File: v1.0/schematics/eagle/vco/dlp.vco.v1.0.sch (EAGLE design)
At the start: 101 parts, among them IC1 NTE912P, IC2 TL074P, IC3 4013N, IC4 TL074P, IC5 TL074P, IC7 TL074P, J1 PWM, J10 SW OUT, J2 LIN FM, J3 SQ OUT, J4 EXP FM, J5 PITCH, J6 SW OUT, J7 SUB OUT, J8 OSC1 OUT, J9 EXP FM, Q1 2N3417, Q2 2N3417, Q3 2N3906, Q4 2N3417, Q5 2N3417, Q6 2N3906

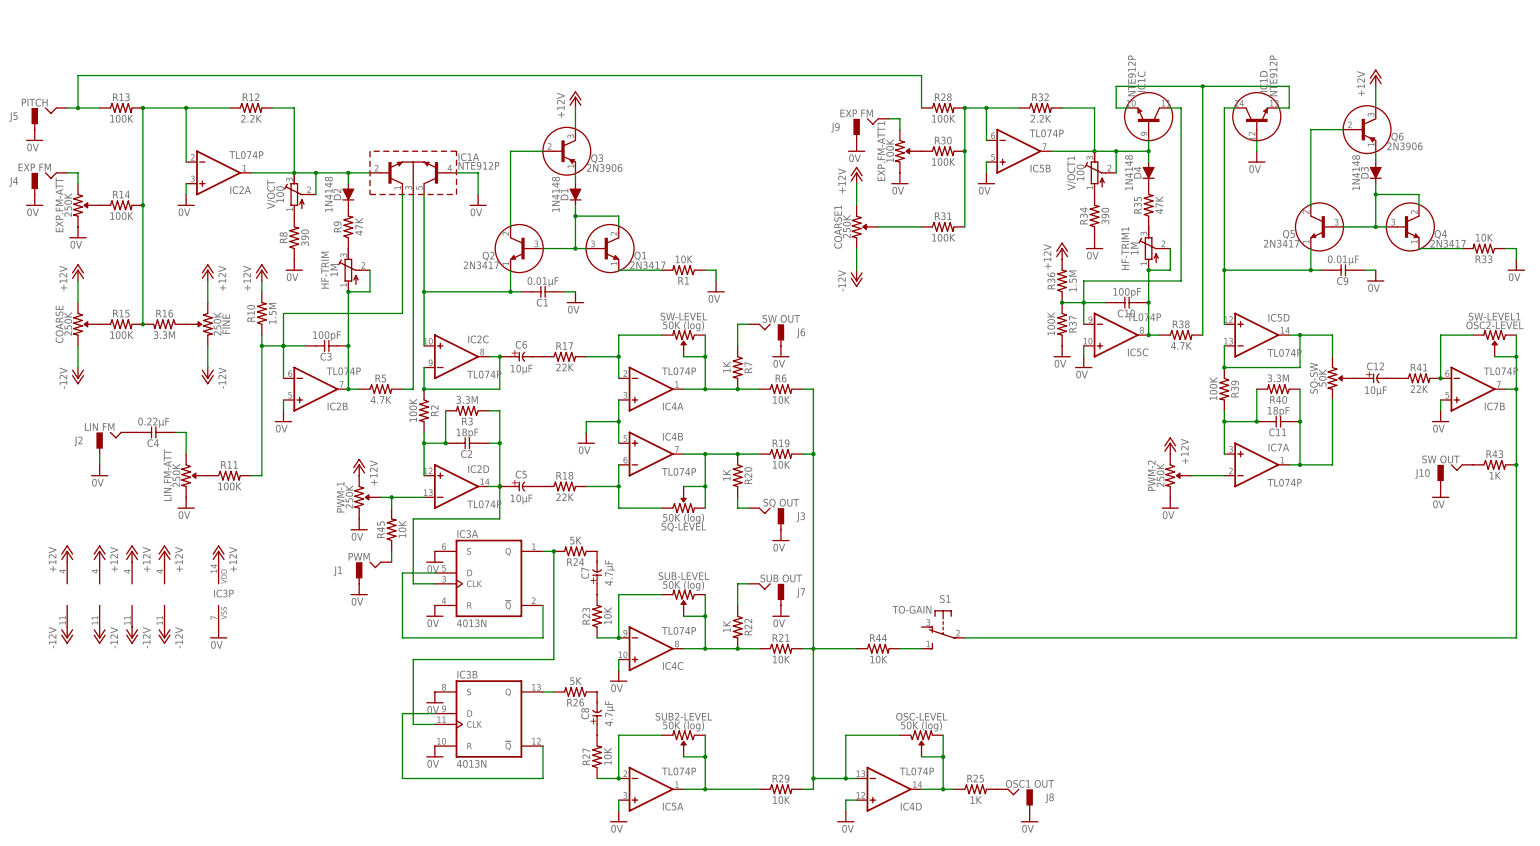
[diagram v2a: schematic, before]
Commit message: Refreshed ASDR pdf (removed png) Updated VCO values Added Pitch Link to VCO Replaced OSC2 LOG.FM with LIN.FM Updated PDF (removed png)
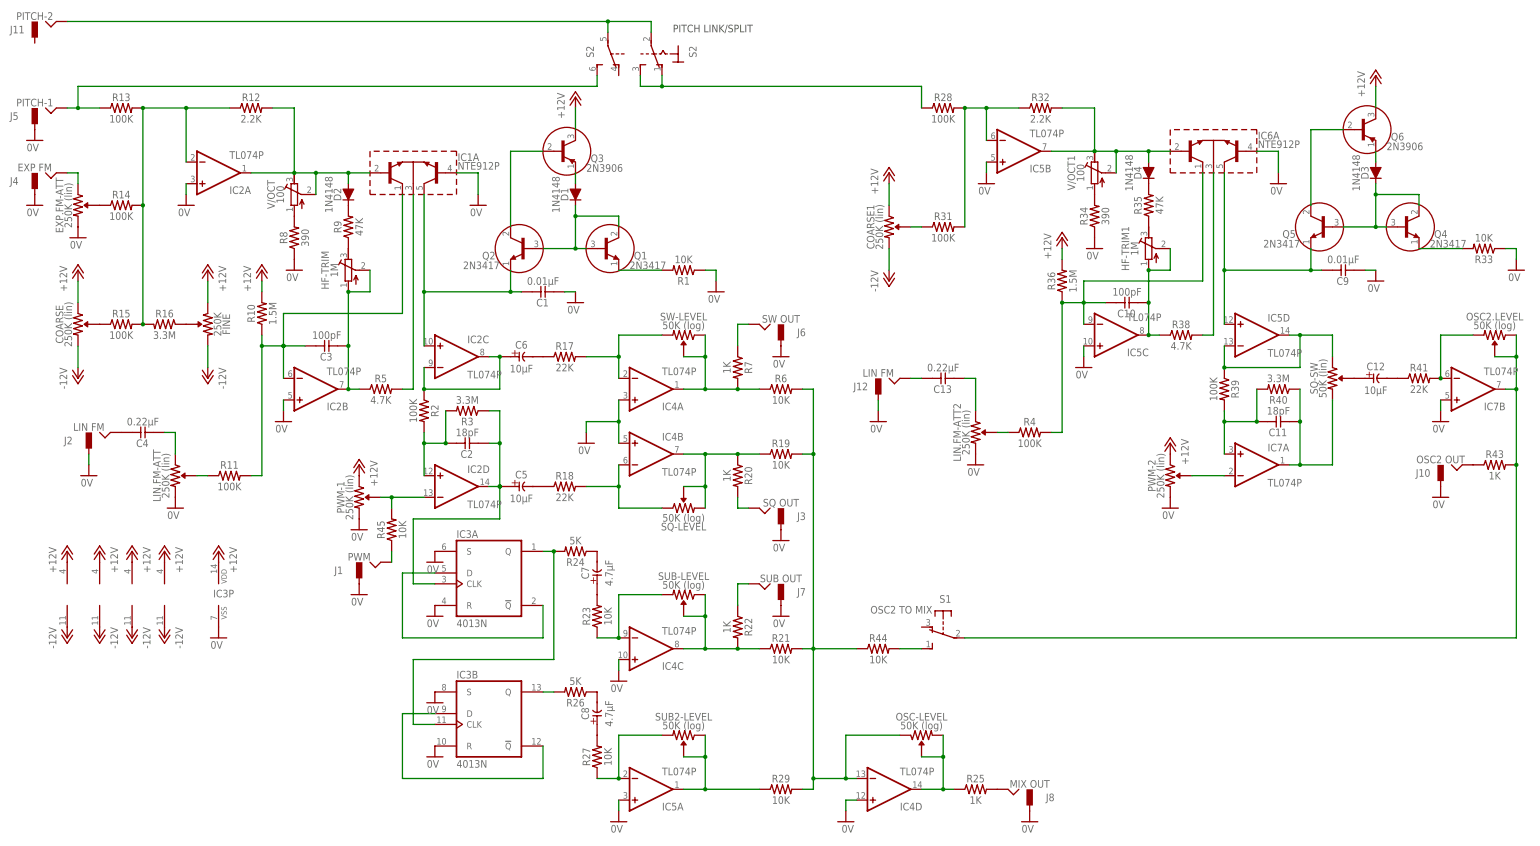
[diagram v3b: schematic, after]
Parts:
- removed EXP.FM-ATT1: 100K, _common:R-VAR
- removed J9: EXP FM, _common:JACK-M
- removed R30, R37: 100K, _common:R0309/10
- added C13: 0.22μF, _common:CC-US025-024X044
- added IC6: NTE912P, _common:NTE912P
- added J11: PITCH-2, _common:JACK-M
- added J12: LIN FM, _common:JACK-M
- added LIN.FM-ATT2: 250K (lin), _common:R-VAR
- added R4: 100K, _common:R0309/10
- added S2: (no value), switch:320-938
- COARSE, COARSE1, EXP.FM-ATT, LIN.FM-ATT, PWM-1, PWM-2: value 250K -> 250K (lin)
- J10: value SW OUT -> OSC2 OUT
- J5: value PITCH -> PITCH-1
- J8: value OSC1 OUT -> MIX OUT
- OSC2.LEVEL: value OSC2-LEVEL -> 50K (log)
- S1: value TO-GAIN -> OSC2 TO MIX
- SQ-SW: value 50K -> 50K (lin)
- renumbered SW-LEVEL1 to OSC2.LEVEL
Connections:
- removed net N$53: EXP.FM-ATT1.1, J9.HOT
- new net N$78: J5.HOT, R13.1, S2B.S
- new net N$79: R28.1, S21.O, S21.S
- new net N$80: LIN.FM-ATT2.P$1, R4.1
- new net N$81: C13.2, LIN.FM-ATT2.1
- net 0V: now also IC6A.B3, J12.GND, LIN.FM-ATT2.2; no longer EXP.FM-ATT1.2, IC1D.B, J9.GND, R37.2
- net N$27: now also J11.HOT, S21.P, S2B.P; no longer J5.HOT, R13.1, R28.1
- net N$51: now also C13.1, J12.HOT; no longer EXP.FM-ATT1.P$1, R30.1
- net N$54: no longer R30.2
- net N$56: no longer IC1D.C
- net N$62: now also IC6A.E; no longer IC1C.E, IC1D.E
- net N$64: now also R4.2; no longer IC1C.C, R37.1
- net N$65: now also IC6A.B1; no longer IC1C.B
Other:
- note added: "PITCH LINK/SPLIT"
- moved on the sheet: C4, COARSE1, J2, LIN.FM-ATT

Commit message: Updated VCO with revised values and added bypass capacitors
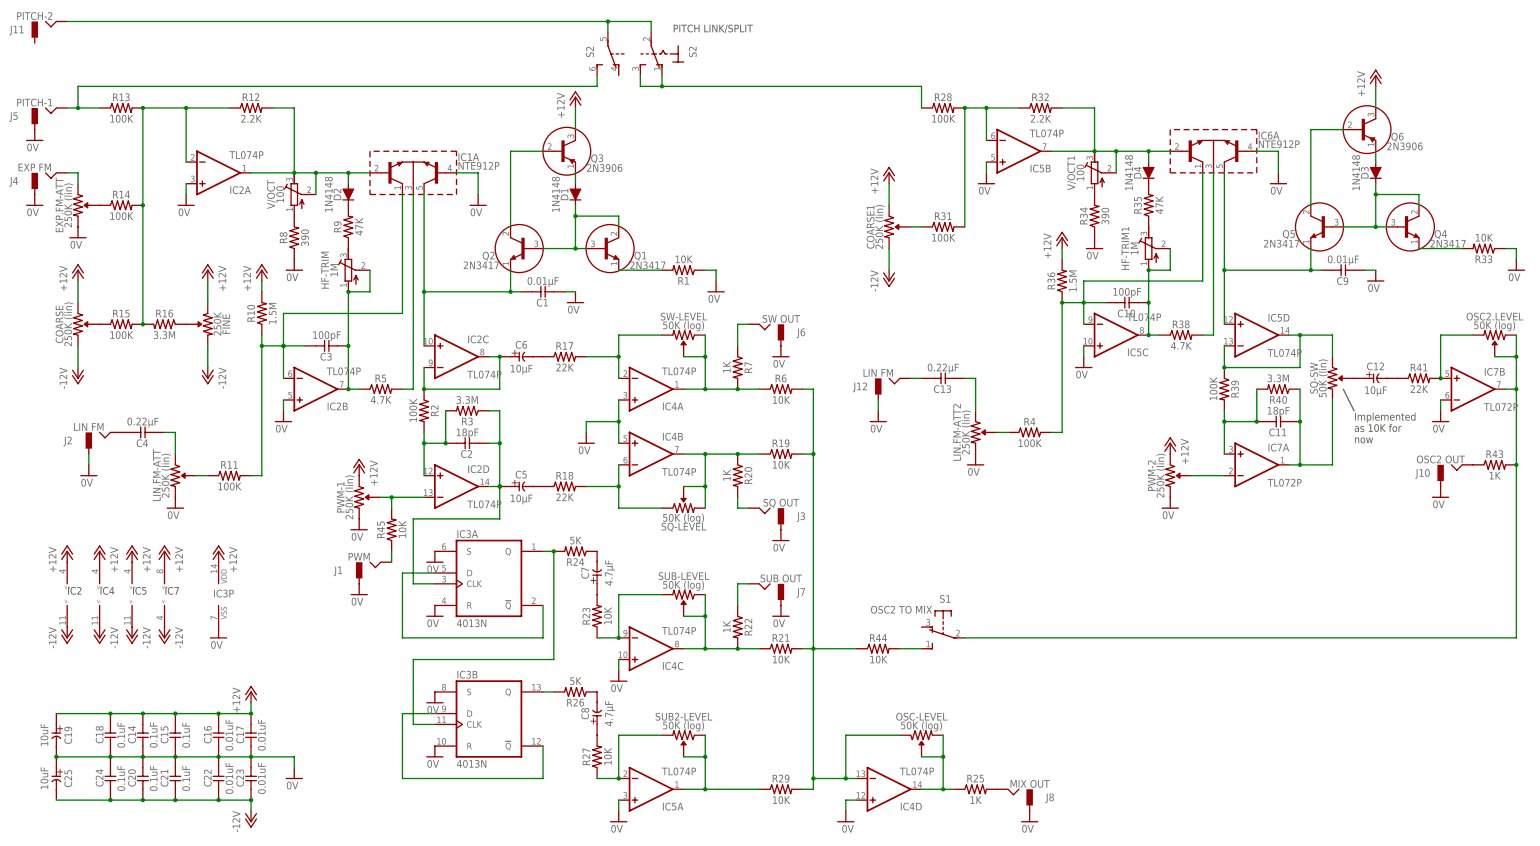
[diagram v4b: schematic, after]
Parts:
- added C14, C15, C18, C20, C21, C24: 0.1uF, _common:CC-US025-024X044
- added C16, C17, C22, C23: 0.01uF, _common:CC-US025-024X044
- added C19, C25: 10uF, _common:CE-USE2-5
- IC7: value TL074P -> TL072P; device _common:TL074P -> _common:TL072P
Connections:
- net +12V: now also C14.1, C15.1, C16.1, C17.1, C18.1, C19.+
- net -12V: now also C20.2, C21.2, C22.2, C23.2, C24.2, C25.-
- net 0V: now also C14.2, C15.2, C16.2, C17.2, C18.2, C19.-, C20.1, C21.1, C22.1, C23.1, C24.1, C25.+, IC7B.-IN; no longer IC7B.+IN
- net N$73: now also IC7B.+IN; no longer IC7B.-IN
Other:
- note added: "IC2"
- note added: "IC4"
- note added: "IC5"
- note added: "IC7"
- note added: "Implemented as 10K for now"
- moved on the sheet: IC7B

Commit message: Corrected errors on VCO across all versions (board needs to be regenerated)
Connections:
- new net N$53: D2.A, IC1A.B1, V/OCT.S
- new net N$71: D4.A, IC6A.B1, V/OCT1.S
- net 0V: now also IC7B.+IN; no longer IC7B.-IN
- net N$16: no longer D2.A, IC1A.B1, V/OCT.S
- net N$65: no longer D4.A, IC6A.B1, V/OCT1.S
- net N$73: now also IC7B.-IN; no longer IC7B.+IN
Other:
- moved on the sheet: IC7B
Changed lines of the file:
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@@
 <?xml version="1.0" encoding="utf-8"?>
 <!DOCTYPE eagle SYSTEM "eagle.dtd">
-<eagle version="6.5.0">
+<eagle version="7.2.0">
 <drawing>
 <settings>
@@
 <instance part="C25" gate="G$1" x="-63.5" y="-73.66" rot="MR0"/>
 <instance part="IC7" gate="A" x="218.44" y="0"/>
-<instance part="IC7" gate="B" x="269.24" y="17.78"/>
 <instance part="IC7" gate="P" x="-38.1" y="-30.48"/>
+<instance part="IC7" gate="B" x="269.24" y="17.78" rot="MR180"/>
 </instances>
 <busses>
@@
 <pinref part="GND37" gate="1" pin="0V"/>
 <wire x1="261.62" y1="15.24" x2="261.62" y2="12.7" width="0.1524" layer="91"/>
-<pinref part="IC7" gate="B" pin="-IN"/>
+<pinref part="IC7" gate="B" pin="+IN"/>
 </segment>
 <segment>
@@
 <net name="N$16" class="0">
 <segment>
-<pinref part="IC1" gate="A" pin="B1"/>
-<wire x1="-2.54" y1="63.5" x2="-2.54" y2="68.58" width="0.1524" layer="91"/>
-<wire x1="-2.54" y1="68.58" x2="5.08" y2="68.58" width="0.1524" layer="91"/>
-<pinref part="D2" gate="G$1" pin="A"/>
-<wire x1="10.16" y1="68.58" x2="5.08" y2="68.58" width="0.1524" layer="91"/>
-<wire x1="5.08" y1="68.58" x2="5.08" y2="66.04" width="0.1524" layer="91"/>
-<junction x="5.08" y="68.58"/>
 <pinref part="IC2" gate="A" pin="OUT"/>
 <wire x1="-17.78" y1="68.58" x2="-7.62" y2="68.58" width="0.1524" layer="91"/>
@@
 <wire x1="-7.62" y1="83.82" x2="-7.62" y2="68.58" width="0.1524" layer="91"/>
 <junction x="-7.62" y="68.58"/>
-<wire x1="-2.54" y1="68.58" x2="-7.62" y2="68.58" width="0.1524" layer="91"/>
-<junction x="-2.54" y="68.58"/>
 <pinref part="V/OCT" gate="G$1" pin="A"/>
-<pinref part="V/OCT" gate="G$1" pin="S"/>
 </segment>
 </net>
@@
 <net name="N$65" class="0">
 <segment>
-<wire x1="185.42" y1="68.58" x2="185.42" y2="73.66" width="0.1524" layer="91"/>
-<wire x1="185.42" y1="73.66" x2="180.34" y2="73.66" width="0.1524" layer="91"/>
 <pinref part="V/OCT1" gate="G$1" pin="A"/>
-<pinref part="V/OCT1" gate="G$1" pin="S"/>
 <pinref part="R32" gate="G$1" pin="2"/>
 <wire x1="172.72" y1="83.82" x2="180.34" y2="83.82" width="0.1524" layer="91"/>
@@
 <wire x1="180.34" y1="73.66" x2="170.18" y2="73.66" width="0.1524" layer="91"/>
 <junction x="180.34" y="73.66"/>
-<pinref part="D4" gate="G$1" pin="A"/>
-<wire x1="193.04" y1="73.66" x2="193.04" y2="71.12" width="0.1524" layer="91"/>
-<wire x1="185.42" y1="73.66" x2="193.04" y2="73.66" width="0.1524" layer="91"/>
-<junction x="185.42" y="73.66"/>
-<pinref part="IC6" gate="A" pin="B1"/>
-<wire x1="193.04" y1="73.66" x2="198.12" y2="73.66" width="0.1524" layer="91"/>
-<junction x="193.04" y="73.66"/>
 </segment>
 </net>
@@
 <pinref part="OSC2.LEVEL" gate="G$1" pin="2"/>
 <wire x1="261.62" y1="30.48" x2="269.24" y2="30.48" width="0.1524" layer="91"/>
-<pinref part="IC7" gate="B" pin="+IN"/>
+<pinref part="IC7" gate="B" pin="-IN"/>
 <junction x="261.62" y="20.32"/>
 </segment>
@@
 </segment>
 </net>
+<net name="N$53" class="0">
+<segment>
+<pinref part="D2" gate="G$1" pin="A"/>
+<pinref part="IC1" gate="A" pin="B1"/>
+<wire x1="10.16" y1="68.58" x2="5.08" y2="68.58" width="0.1524" layer="91"/>
+<wire x1="5.08" y1="68.58" x2="5.08" y2="66.04" width="0.1524" layer="91"/>
+<junction x="5.08" y="68.58"/>
+<wire x1="-2.54" y1="68.58" x2="5.08" y2="68.58" width="0.1524" layer="91"/>
+<wire x1="-2.54" y1="63.5" x2="-2.54" y2="68.58" width="0.1524" layer="91"/>
+<pinref part="V/OCT" gate="G$1" pin="S"/>
+</segment>
+</net>
+<net name="N$71" class="0">
+<segment>
+<pinref part="IC6" gate="A" pin="B1"/>
+<pinref part="D4" gate="G$1" pin="A"/>
+<wire x1="193.04" y1="73.66" x2="193.04" y2="71.12" width="0.1524" layer="91"/>
+<wire x1="193.04" y1="73.66" x2="198.12" y2="73.66" width="0.1524" layer="91"/>
+<junction x="193.04" y="73.66"/>
+<wire x1="185.42" y1="73.66" x2="193.04" y2="73.66" width="0.1524" layer="91"/>
+<wire x1="185.42" y1="68.58" x2="185.42" y2="73.66" width="0.1524" layer="91"/>
+<pinref part="V/OCT1" gate="G$1" pin="S"/>
+</segment>
+</net>
